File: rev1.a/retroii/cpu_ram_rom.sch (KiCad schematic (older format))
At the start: 40 parts, among them J23 Conn_01x02, U10 74LS08, U18 74LS04, U6 AT28C256_EEPROM, U8 IDT7008_Dual_Port_RAM, U9 74LS32, Y2 ECS-2100X-1MHZ

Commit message: added ram plcc84 footprint and 3d model.
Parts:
- U8: footprint (none) -> retroii_footprints:Assman_PLCC84_ACCS084GT
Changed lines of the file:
@@
 F 0 "U8" H 9220 2140 60  0000 C CNN
 F 1 "IDT7008_Dual_Port_RAM" H 10880 7595 60  0000 C CNN
-F 2 "" H 11175 6840 60  0001 C CNN
+F 2 "retroii_footprints:Assman_PLCC84_ACCS084GT" H 11175 6840 60  0001 C CNN
 F 3 "https://www.mouser.com/datasheet/2/464/IDT_7008_DST_20180322-1485473.pdf" H 10225 7837 60  0001 C CNN
 	1    10225 4840

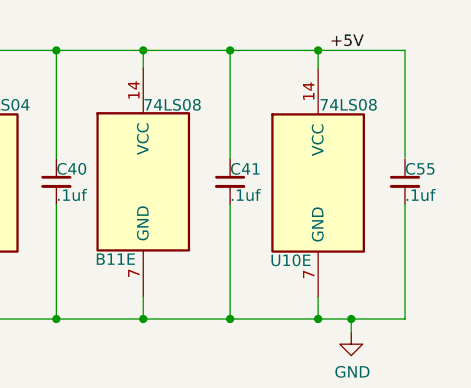
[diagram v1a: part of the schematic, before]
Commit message: replaced 558 quad timer with 2 556 dual timers.
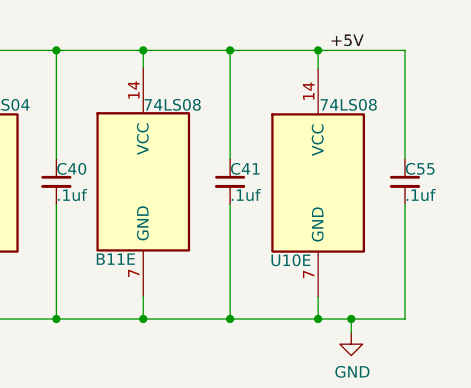
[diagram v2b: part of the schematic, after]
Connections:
- net +5V: now also C55.1
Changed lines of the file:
@@
 	15735 2080 15735 1580
 Connection ~ 15500 2080
-Wire Wire Line
-	15735 1375 15735 905
-Wire Wire Line
-	15355 905  15735 905
 $Comp
 L Connector_Generic:Conn_01x02 J23
@@
 Text Label 4625 7960 2    50   ~ 0
 Clock
+Wire Wire Line
+	15735 905  15735 1380
+Wire Wire Line
+	15355 905  15735 905
 Wire Bus Line
 	6225 1590 6225 3190

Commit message: more layout
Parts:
- added R?: 3.3K, retroii_footprints:R_Axial_DIN0207_L6.3mm_D2.5mm_P10.16mm_Horizontal, symbol 6502:R
- R55: value 0 -> DNP
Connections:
- net RDY: now also R?.2; no longer H7.2 (RDY)
- new net: H7.2 (RDY), R?.1
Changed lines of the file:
@@
 Wire Wire Line
 	3890 3890 4575 3890
-Text HLabel 4575 2390 0    50   Input ~ 0
+Text HLabel 4275 2390 0    50   Input ~ 0
 RDY
 Text HLabel 4575 2540 0    50   Output ~ 0
@@
 P 4390 2240
 F 0 "R55" V 4315 2240 50  0000 C CNN
-F 1 "0" V 4390 2240 50  0000 C CNN
+F 1 "DNP" V 4390 2240 50  0000 C CNN
 F 2 "retroii_footprints:R_Axial_DIN0207_L6.3mm_D2.5mm_P10.16mm_Horizontal" V 4320 2240 30  0001 C CNN
 F 3 "" H 4390 2240 30  0000 C CNN
@@
 	4540 2240 4575 2240
 Wire Wire Line
-	4240 2240 4155 2240
-Wire Wire Line
-	4155 2240 4155 2315
+	3885 2240 3885 2315
 $Comp
 L 6502Bootstrapper-cache:GND #PWR0101
 U 1 1 5CF69118
-P 4155 2315
-F 0 "#PWR0101" H 4155 2065 50  0001 C CNN
-F 1 "GND" H 4160 2142 50  0000 C CNN
-F 2 "" H 4155 2315 60  0000 C CNN
-F 3 "" H 4155 2315 60  0000 C CNN
-	1    4155 2315
+P 3885 2315
+F 0 "#PWR0101" H 3885 2065 50  0001 C CNN
+F 1 "GND" H 3890 2142 50  0000 C CNN
+F 2 "" H 3885 2315 60  0000 C CNN
+F 3 "" H 3885 2315 60  0000 C CNN
+	1    3885 2315
 	1    0    0    -1
 $EndComp
@@
 Wire Wire Line
 	15355 905  15735 905
+$Comp
+L 6502:R R?
+U 1 1 5CEFFCAA
+P 4425 2390
+F 0 "R?" V 4350 2390 50  0000 C CNN
+F 1 "3.3K" V 4425 2390 50  0000 C CNN
+F 2 "retroii_footprints:R_Axial_DIN0207_L6.3mm_D2.5mm_P10.16mm_Horizontal" V 4355 2390 30  0001 C CNN
+F 3 "" H 4425 2390 30  0000 C CNN
+	1    4425 2390
+	0    1    1    0
+$EndComp
+Wire Wire Line
+	3885 2240 4240 2240
 Wire Bus Line
 	6225 1590 6225 3190

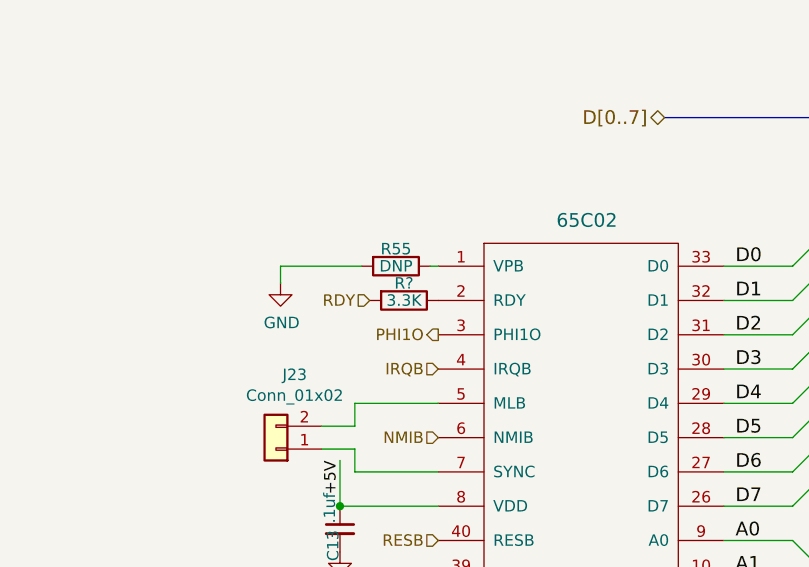
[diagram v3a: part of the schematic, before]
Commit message: added more in/out caps for psu. finished initial layout of psu.
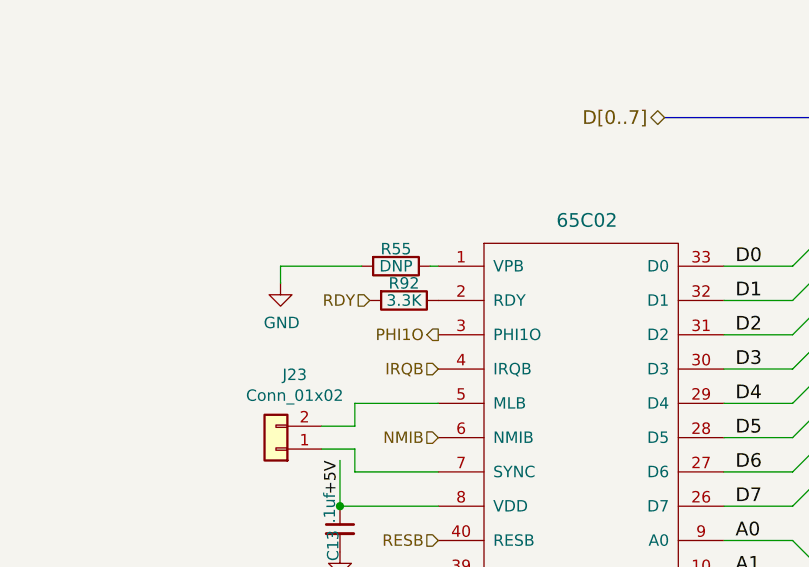
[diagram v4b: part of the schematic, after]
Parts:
- gave numbers to parts that had none: 1
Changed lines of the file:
@@
 	15355 905  15735 905
 $Comp
-L 6502:R R?
+L 6502:R R92
 U 1 1 5CEFFCAA
 P 4425 2390
-F 0 "R?" V 4350 2390 50  0000 C CNN
+F 0 "R92" V 4350 2390 50  0000 C CNN
 F 1 "3.3K" V 4425 2390 50  0000 C CNN
 F 2 "retroii_footprints:R_Axial_DIN0207_L6.3mm_D2.5mm_P10.16mm_Horizontal" V 4355 2390 30  0001 C CNN

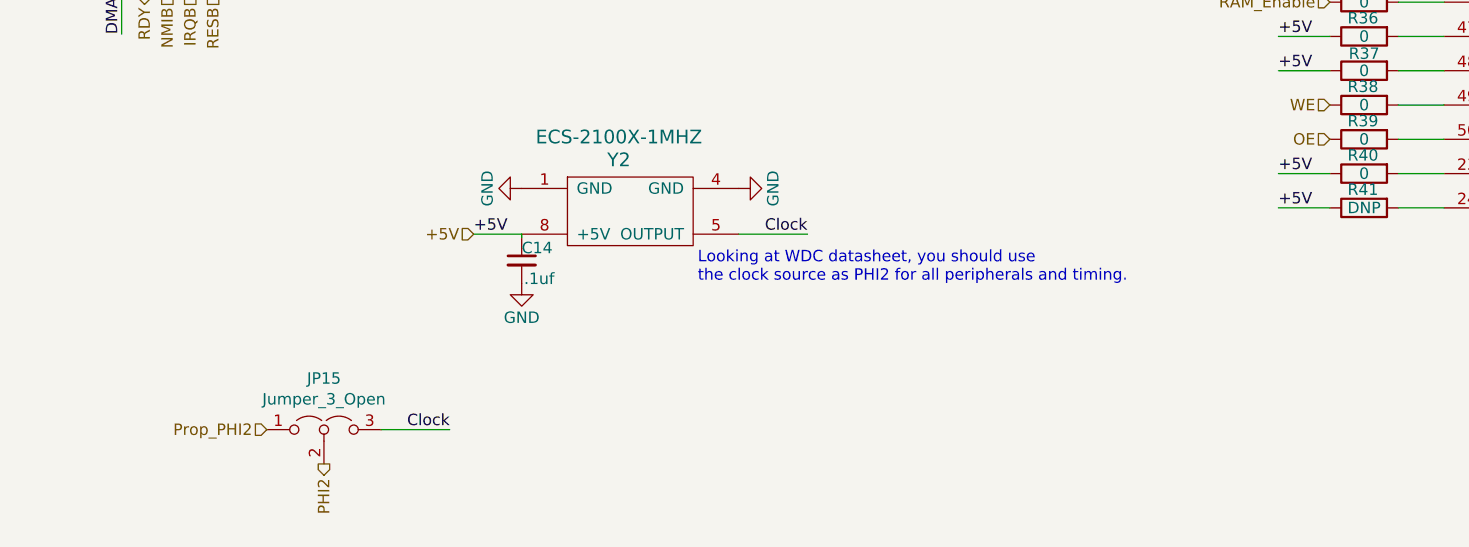
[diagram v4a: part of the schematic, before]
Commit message: modified prop layout to include jumpers for phi2, rdy, and dma.
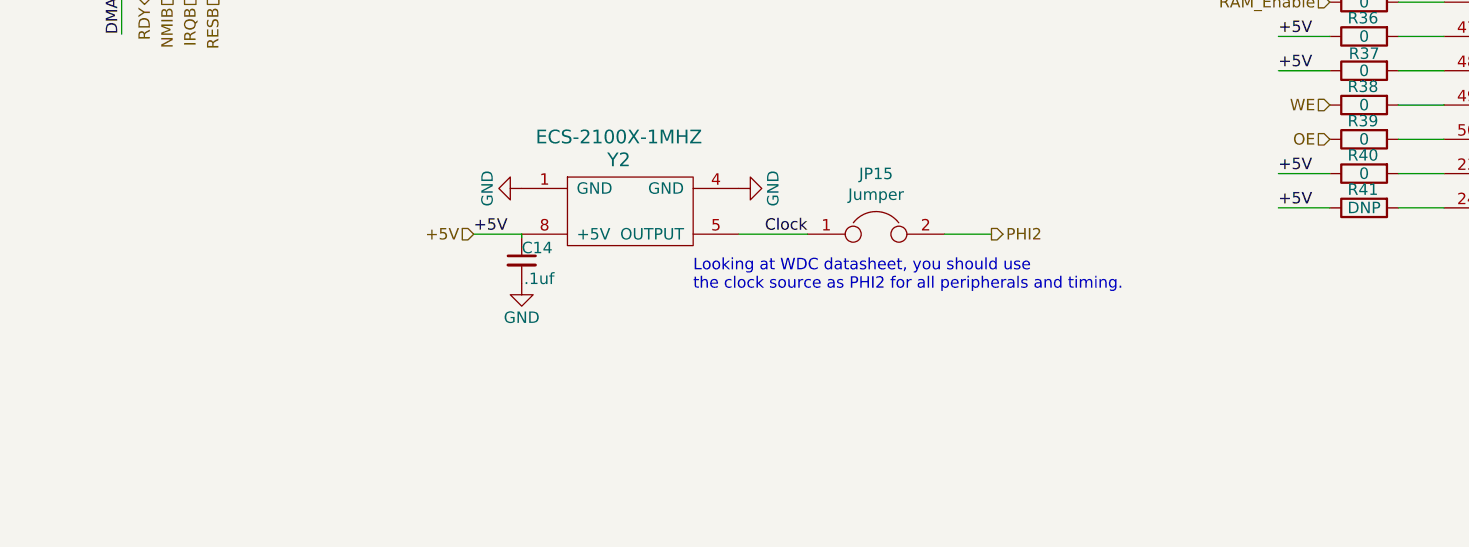
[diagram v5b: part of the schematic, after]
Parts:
- removed JP15: Jumper_3_Open, Connector_PinHeader_2.54mm:PinHeader_1x03_P2.54mm_Vertical, symbol Jumper:Jumper_3_Open
- added JP15: Jumper, Connector_PinHeader_2.54mm:PinHeader_1x02_P2.54mm_Vertical, symbol Device:Jumper
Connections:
- net Clock: now also JP15.1
- net PHI2: now also JP15.2
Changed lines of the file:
@@
 Text HLabel 3290 3790 0    50   Input ~ 0
 PHI2
-Text Notes 5710 7320 0    50   ~ 0
+Text Notes 5690 7355 0    50   ~ 0
 Looking at WDC datasheet, you should use \nthe clock source as PHI2 for all peripherals and timing.
 NoConn ~ 4575 3590
@@
 Wire Wire Line
 	4210 3140 4575 3140
-Text HLabel 3825 7960 0    50   Input ~ 0
-Prop_PHI2
-$Comp
-L Jumper:Jumper_3_Open JP15
-U 1 1 5D36A93F
-P 4075 7960
-F 0 "JP15" H 4075 8184 50  0000 C CNN
-F 1 "Jumper_3_Open" H 4075 8093 50  0000 C CNN
-F 2 "Connector_PinHeader_2.54mm:PinHeader_1x03_P2.54mm_Vertical" H 4075 7960 50  0001 C CNN
-F 3 "~" H 4075 7960 50  0001 C CNN
-	1    4075 7960
-	1    0    0    -1
-$EndComp
-Text HLabel 4075 8110 3    50   Output ~ 0
+Text HLabel 6995 7105 2    50   Output ~ 0
 PHI2
-Wire Wire Line
-	4625 7960 4325 7960
-Text Label 4625 7960 2    50   ~ 0
-Clock
 Wire Wire Line
 	15735 905  15735 1380
@@
 Wire Wire Line
 	3885 2240 4240 2240
+$Comp
+L Device:Jumper JP15
+U 1 1 5D791E9F
+P 6490 7105
+F 0 "JP15" H 6490 7369 50  0000 C CNN
+F 1 "Jumper" H 6490 7278 50  0000 C CNN
+F 2 "Connector_PinHeader_2.54mm:PinHeader_1x02_P2.54mm_Vertical" H 6490 7105 50  0001 C CNN
+F 3 "~" H 6490 7105 50  0001 C CNN
+	1    6490 7105
+	1    0    0    -1
+$EndComp
+Wire Wire Line
+	6790 7105 6995 7105
 Wire Bus Line
 	6225 1590 6225 3190
